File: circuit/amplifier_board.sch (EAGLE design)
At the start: 21 parts

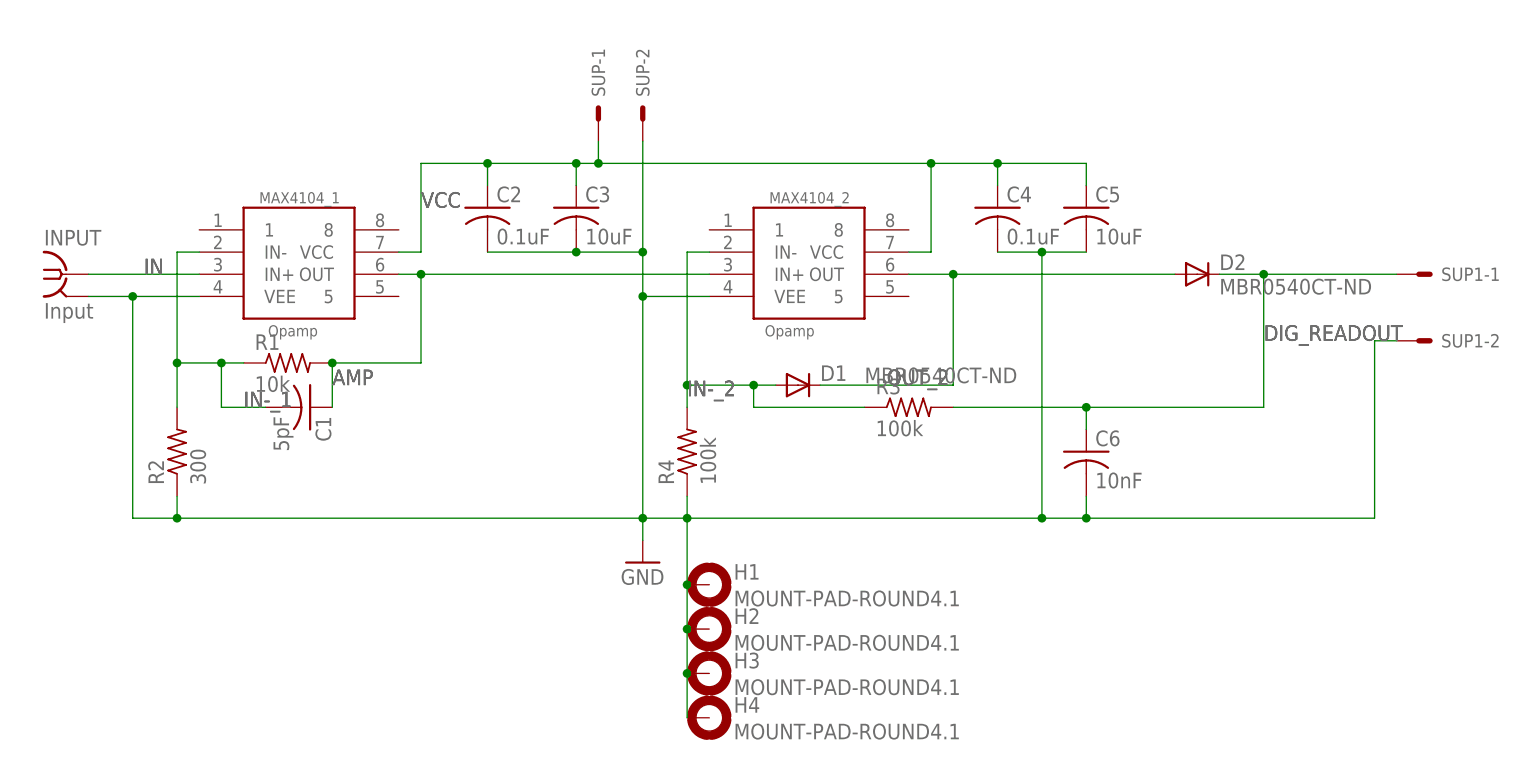
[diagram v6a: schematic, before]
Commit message: boards: Added VEE line to header.  Corrected header to be 0.100", (what we have in stock,) not 2mm header.
Also added filtering caps (backwards, sort of,) to stabilize the VEE line.
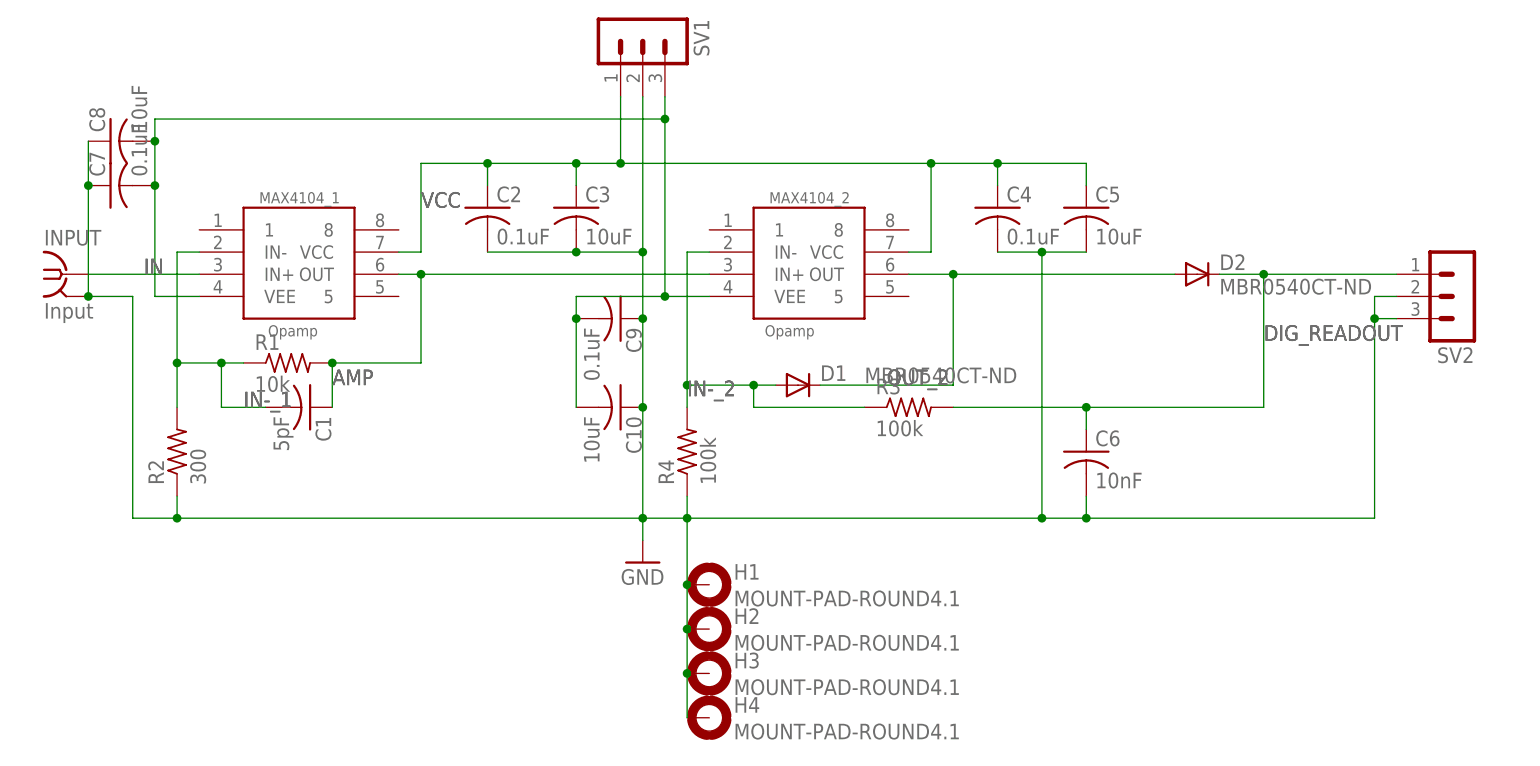
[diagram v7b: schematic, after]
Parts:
- removed SUP, SUP1: 332-02, con-garry:332-02
- added C10, C8: 10uF, rcl:C-USC0603
- added C7, C9: 0.1uF, rcl:C-USC0603
- added SV1, SV2: (no value), con-lstb:MA03-1
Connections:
- new net VEE: C10.2, C7.2, C8.2, C9.2, MAX4104_1.VEE, MAX4104_2.VEE, SV1.3
- net DIG_READOUT: now also SV2.1; no longer SUP1-1.S
- net GND: now also C10.1, C7.1, C8.1, C9.1, SV1.2, SV2.2, SV2.3; no longer MAX4104_1.VEE, MAX4104_2.VEE, SUP-2.S, SUP1-2.S
- net VCC: now also SV1.1; no longer SUP-1.S
